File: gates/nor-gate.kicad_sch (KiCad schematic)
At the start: 7 parts, among them Q1 NPN, Q2 NPN, Q3 NPN

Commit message: Schematic for register
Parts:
- removed Q1, Q2, Q3: NPN, symbol Simulation_SPICE:NPN
- removed R4, R5: 10k, symbol Device:R
- removed R6, R7: 4.7k, symbol Device:R
- added Q8, Q9: NPN, symbol Simulation_SPICE:NPN
- added R11, R12: 10k, symbol Device:R
- added R13: 4.7k, symbol Device:R
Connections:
- net +5V: now also R13.1
- net A: now also R12.1
- net B: now also R11.1
- net GND: now also Q8.3 (E), Q9.3 (E)
- net OUTPUT: now also Q8.1 (C), Q9.1 (C), R13.2
- new net: Q9.2 (B), R11.2
- new net: Q8.2 (B), R12.2

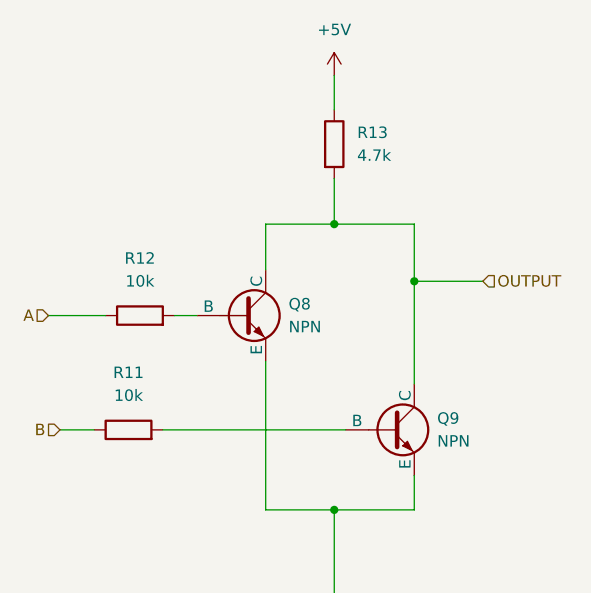
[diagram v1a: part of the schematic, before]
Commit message: Use IC circuits in adder circuit
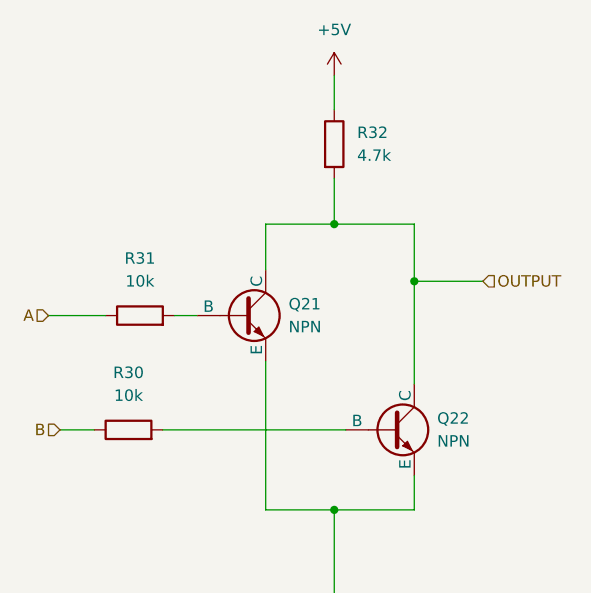
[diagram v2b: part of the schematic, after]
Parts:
- renumbered Q8 to Q21, Q9 to Q22, R11 to R30, R12 to R31, R13 to R32
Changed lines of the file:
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@@
 		(dnp no)
 		(fields_autoplaced yes)
-		(property "Reference" "R13"
+		(property "Reference" "R32"
 			(at 123.19 53.3399 0)
 			(effects
@@
 		(dnp no)
 		(fields_autoplaced yes)
-		(property "Reference" "#PWR016"
+		(property "Reference" "#PWR032"
 			(at 120.65 115.57 0)
 			(effects
@@
 		(dnp no)
 		(fields_autoplaced yes)
-		(property "Reference" "Q9"
+		(property "Reference" "Q22"
 			(at 132.08 85.0899 0)
 			(effects
@@
 		(dnp no)
 		(fields_autoplaced yes)
-		(property "Reference" "R11"
+		(property "Reference" "R30"
 			(at 97.79 80.01 90)
 			(effects
@@
 		(dnp no)
 		(fields_autoplaced yes)
-		(property "Reference" "Q8"
+		(property "Reference" "Q21"
 			(at 115.57 72.3899 0)
 			(effects
@@
 		(dnp no)
 		(fields_autoplaced yes)
-		(property "Reference" "#PWR015"
+		(property "Reference" "#PWR031"
 			(at 120.65 50.8 0)
 			(effects
@@
 		(dnp no)
 		(fields_autoplaced yes)
-		(property "Reference" "R12"
+		(property "Reference" "R31"
 			(at 99.06 67.31 90)
 			(effects
